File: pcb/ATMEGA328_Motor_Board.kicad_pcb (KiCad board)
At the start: 2 copper layers, 77 x 100 mm, 182 parts, among them P1 CONN_01X04, P10 CONN_01X04, P11 CONN_01X02, P12 CONN_01X03, P13 CONN_01X02, P14 USB_MINI, P15 CONN_01X02, P16 CONN_02X03, P2 CONN_01X04, P3 CONN_01X03, P4 CONN_01X03, P5 CONN_01X03, P6 CONN_01X03, P7 CONN_01X03, P8 CONN_01X03, P9 CONN_01X04, SW1 Pulsador_2p, U1 ATMEGA328, U10 VOM617A, U11 VOM617A, U12 ASSR-1218, U13 ASSR-1218, U2 PCA9685, U3 FT231X, U4 L298P, U5 L298P, U6 TSR_1, U7 LM2903, U8 LM2903, U9 VOM617A, Y1 16MHz

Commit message: finalizado conexionado de pads
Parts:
- removed the Gnd-Via at (123.2, 111.3)
- added Gnd-Via: VAL**, Vias:Gnd-Via, F.Cu at (164.8, 121.6)
- added Gnd-Via: VAL**, Vias:Gnd-Via, F.Cu at (137.4, 83.2)
- added Gnd-Via: VAL**, Vias:Gnd-Via, F.Cu at (175.9, 86.8)
- added Gnd-Via: VAL**, Vias:Gnd-Via, F.Cu at (128.4, 97.7)
- added Gnd-Via: VAL**, Vias:Gnd-Via, F.Cu at (167.9, 99.3)
- added Gnd-Via: VAL**, Vias:Gnd-Via, F.Cu at (167.9, 97.8)
- added Gnd-Via: VAL**, Vias:Gnd-Via, F.Cu at (152.7, 101.4)
- added Gnd-Via: VAL**, Vias:Gnd-Via, F.Cu at (158.1, 64.3)
- added Gnd-Via: VAL**, Vias:Gnd-Via, F.Cu at (165.6, 69.8)
- added Gnd-Via: VAL**, Vias:Gnd-Via, F.Cu at (111.3, 48.2)
- added Gnd-Via: VAL**, Vias:Gnd-Via, F.Cu at (117.1, 69.5)
- added Gnd-Via: VAL**, Vias:Gnd-Via, F.Cu at (157.6, 121.5)
- added Gnd-Via: VAL**, Vias:Gnd-Via, F.Cu at (114.8, 63.6)
- added Gnd-Via: VAL**, Vias:Gnd-Via, F.Cu at (143.9, 48.4)
- added Gnd-Via: VAL**, Vias:Gnd-Via, F.Cu at (157.0, 47.3)
- added Gnd-Via: VAL**, Vias:Gnd-Via, F.Cu at (121.7, 115.2)
- added Gnd-Via: VAL**, Vias:Gnd-Via, F.Cu at (173.9, 62.1)
- added Gnd-Via: VAL**, Vias:Gnd-Via, F.Cu at (184.0, 62.1)
- added Gnd-Via: VAL**, Vias:Gnd-Via, F.Cu at (184.0, 54.8)
- added Gnd-Via: VAL**, Vias:Gnd-Via, F.Cu at (184.0, 47.7)
- added Gnd-Via: VAL**, Vias:Gnd-Via, F.Cu at (171.6, 79.2)
- added Gnd-Via: VAL**, Vias:Gnd-Via, F.Cu at (173.6, 79.3)
- added Gnd-Via: VAL**, Vias:Gnd-Via, F.Cu at (162.7, 102.9)
- added Gnd-Via: VAL**, Vias:Gnd-Via, F.Cu at (169.7, 120.0)
- added Gnd-Via: VAL**, Vias:Gnd-Via, F.Cu at (174.0, 113.2)
- added Gnd-Via: VAL**, Vias:Gnd-Via, F.Cu at (174.1, 118.8)
- added Gnd-Via: VAL**, Vias:Gnd-Via, F.Cu at (136.4, 91.0)
- added Gnd-Via: VAL**, Vias:Gnd-Via, F.Cu at (175.6, 89.9)
- added Gnd-Via: VAL**, Vias:Gnd-Via, F.Cu at (182.2, 91.3)
- added Gnd-Via: VAL**, Vias:Gnd-Via, F.Cu at (150.0, 128.6)
- added Gnd-Via: VAL**, Vias:Gnd-Via, F.Cu at (145.8, 83.7)
- added Gnd-Via: VAL**, Vias:Gnd-Via, F.Cu at (140.9, 87.9)
- added Gnd-Via: VAL**, Vias:Gnd-Via, F.Cu at (151.1, 136.0)
- added Gnd-Via: VAL**, Vias:Gnd-Via, F.Cu at (159.7, 102.9)
- added Gnd-Via: VAL**, Vias:Gnd-Via, F.Cu at (151.1, 134.3)
- added Gnd-Via: VAL**, Vias:Gnd-Via, F.Cu at (141.8, 120.5)
- added Gnd-Via: VAL**, Vias:Gnd-Via, F.Cu at (129.2, 122.2)
- added Gnd-Via: VAL**, Vias:Gnd-Via, F.Cu at (125.0, 104.0)
- added Gnd-Via: VAL**, Vias:Gnd-Via, F.Cu at (156.2, 72.3)
- added Gnd-Via: VAL**, Vias:Gnd-Via, F.Cu at (155.4, 74.7)
- added Gnd-Via: VAL**, Vias:Gnd-Via, F.Cu at (144.1, 88.9)
- added Gnd-Via: VAL**, Vias:Gnd-Via, F.Cu at (132.1, 72.7)
- added Gnd-Via: VAL**, Vias:Gnd-Via, F.Cu at (154.2, 83.2)
- added Gnd-Via: VAL**, Vias:Gnd-Via, F.Cu at (159.1, 83.3)
- added Gnd-Via: VAL**, Vias:Gnd-Via, F.Cu at (137.0, 103.0)
- added Gnd-Via: VAL**, Vias:Gnd-Via, F.Cu at (164.4, 83.5)
- added Gnd-Via: VAL**, Vias:Gnd-Via, F.Cu at (128.3, 70.8)
- added Gnd-Via: VAL**, Vias:Gnd-Via, F.Cu at (131.3, 70.9)
- added Gnd-Via: VAL**, Vias:Gnd-Via, F.Cu at (133.0, 103.0)
- added Gnd-Via: VAL**, Vias:Gnd-Via, F.Cu at (122.3, 83.2)
- added Gnd-Via: VAL**, Vias:Gnd-Via, F.Cu at (127.3, 83.2)
- added Gnd-Via: VAL**, Vias:Gnd-Via, F.Cu at (132.3, 83.2)
- moved Gnd-Via 7.17 mm to (153.7, 105.4)
- moved R2 2.50 mm to (145.5, 71.7), turned to 90 degrees
- moved R3 2.50 mm to (148.0, 71.7), turned to 90 degrees
- moved C15 0.90 mm to (123.3, 113.6)
- moved Gnd-Via 0.76 mm to (128.4, 96.3)
- moved R23 0.45 mm to (151.4, 106.9)
- moved R15 0.13 mm to (125.1, 107.1)
- moved P5 0.07 mm to (176.8, 94.9)
- turned R4 to 90 degrees
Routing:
- net +5V: track 301.4 -> 538.4 mm, vias 4 -> 12
- net SERVO4: track 0.00 -> 75.0 mm, vias 0 -> 1
- net SERVO3: track 0.00 -> 72.7 mm, vias 0 -> 1
- net MOTOR4_EN: track 3.01 -> 75.6 mm, vias 0 -> 2
- net SERVO2: track 0.00 -> 59.1 mm, vias 0 -> 1
- net SERVO1: track 0.00 -> 58.3 mm, vias 0 -> 1
- net MOTOR3_EN: track 2.50 -> 60.0 mm, vias 0 -> 2
- net MOTOR2_EN: track 4.19 -> 50.5 mm, vias 1 -> 2
- net Motor3-: track 33.5 -> 77.9 mm, vias 0 -> 2
- net Motor4-: track 30.2 -> 70.7 mm, vias 1 -> 3
- net MOTOR3_SENSE: track 3.51 -> 43.9 mm, vias 0 -> 2
- net MOTOR4_B: track 4.63 -> 44.6 mm, vias 0 -> 2
- net /Potencia/Motor3_B_in: track 10.1 -> 47.5 mm, vias 0 -> 2
- net Motor4+: track 27.3 -> 64.1 mm, vias 0 -> 4
- net RESET: track 23.5 -> 59.8 mm
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
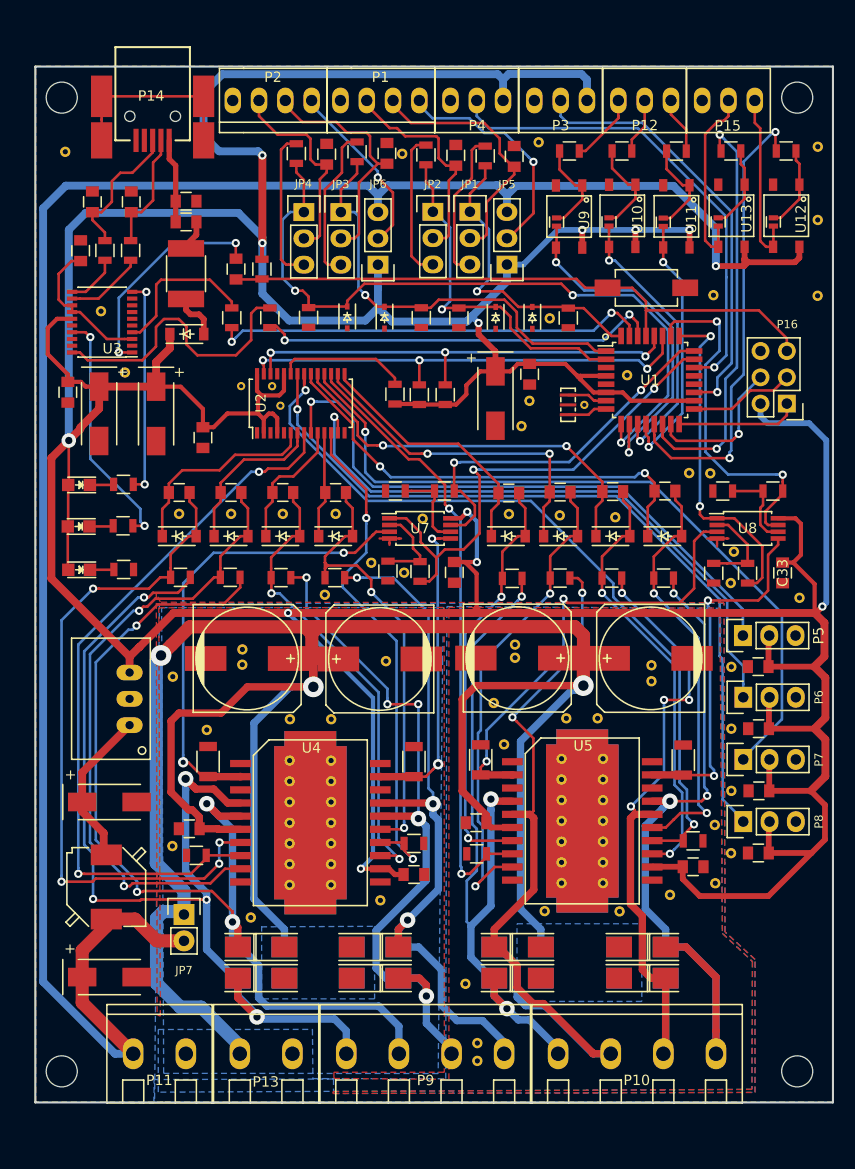
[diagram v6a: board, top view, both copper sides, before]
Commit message: añadidas referencias de componentes a las serigrafias
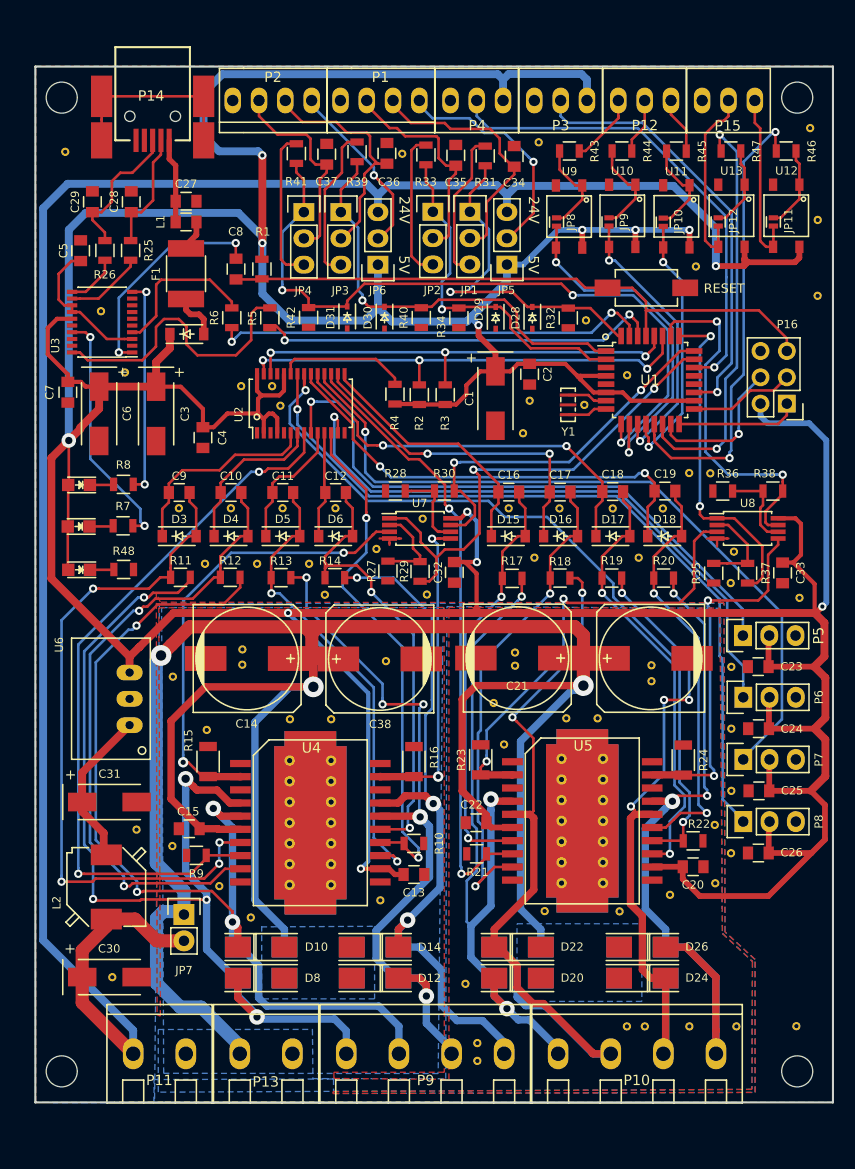
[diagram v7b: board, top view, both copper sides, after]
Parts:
- added Gnd-Via: VAL**, Vias:Gnd-Via, F.Cu at (181.9, 132.6)
- added Gnd-Via: VAL**, Vias:Gnd-Via, F.Cu at (129.9, 88.0)
- added Gnd-Via: VAL**, Vias:Gnd-Via, F.Cu at (124.8, 88.0)
- added Gnd-Via: VAL**, Vias:Gnd-Via, F.Cu at (166.7, 87.4)
- added Gnd-Via: VAL**, Vias:Gnd-Via, F.Cu at (156.6, 87.4)
- added Gnd-Via: VAL**, Vias:Gnd-Via, F.Cu at (169.0, 82.7)
- added Gnd-Via: VAL**, Vias:Gnd-Via, F.Cu at (176.1, 132.7)
- added Gnd-Via: VAL**, Vias:Gnd-Via, F.Cu at (171.6, 132.7)
- added Gnd-Via: VAL**, Vias:Gnd-Via, F.Cu at (167.3, 132.7)
- added Gnd-Via: VAL**, Vias:Gnd-Via, F.Cu at (165.6, 132.7)
- added Gnd-Via: VAL**, Vias:Gnd-Via, F.Cu at (115.9, 127.9)
- added Gnd-Via: VAL**, Vias:Gnd-Via, F.Cu at (118.2, 113.7)
- added Gnd-Via: VAL**, Vias:Gnd-Via, F.Cu at (126.2, 119.1)
- added Gnd-Via: VAL**, Vias:Gnd-Via, F.Cu at (134.9, 88.0)
- moved Gnd-Via 3.51 mm to (161.6, 64.5)
- moved Gnd-Via 3.24 mm to (172.2, 59.3)
- moved Gnd-Via 3.05 mm to (146.2, 91.0)
- moved Gnd-Via 1.95 mm to (183.2, 45.9)
- moved Gnd-Via 1.42 mm to (141.4, 86.6)
- moved Gnd-Via 0.89 mm to (164.2, 82.7)
- moved Gnd-Via 0.77 mm to (154.8, 97.8)
- moved Gnd-Via 0.77 mm to (154.8, 96.6)
- moved Gnd-Via 0.71 mm to (155.5, 75.4)
- moved Gnd-Via 0.67 mm to (159.1, 82.7)
- moved Gnd-Via 0.55 mm to (154.2, 82.7)
- moved Gnd-Via 0.54 mm to (132.3, 82.6)
- moved Gnd-Via 0.54 mm to (137.4, 82.6)
- moved Gnd-Via 0.54 mm to (122.3, 82.6)
- moved Gnd-Via 0.54 mm to (127.3, 82.6)
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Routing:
- net ENC1_A2: track 30.0 -> 34.6 mm
- net Motor1-: track 97.5 -> 95.9 mm
- net Motor2-: track 69.0 -> 70.2 mm
- net /Potencia/Motor2_B_in: track 43.2 -> 44.4 mm
- net MOTOR1_SENSE: track 45.4 -> 44.4 mm
- net +24V: track 198.4 -> 197.5 mm
- net Motor2+: track 68.7 -> 69.4 mm
- net MOTOR2_SENSE: track 30.1 -> 30.8 mm
- net ENC2_A: track 23.2 -> 22.7 mm
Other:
- board text added: "24V"
- board text added: "5V"
- board text added: "RESET"

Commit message: añadida descripcion de terminales en serigrafia
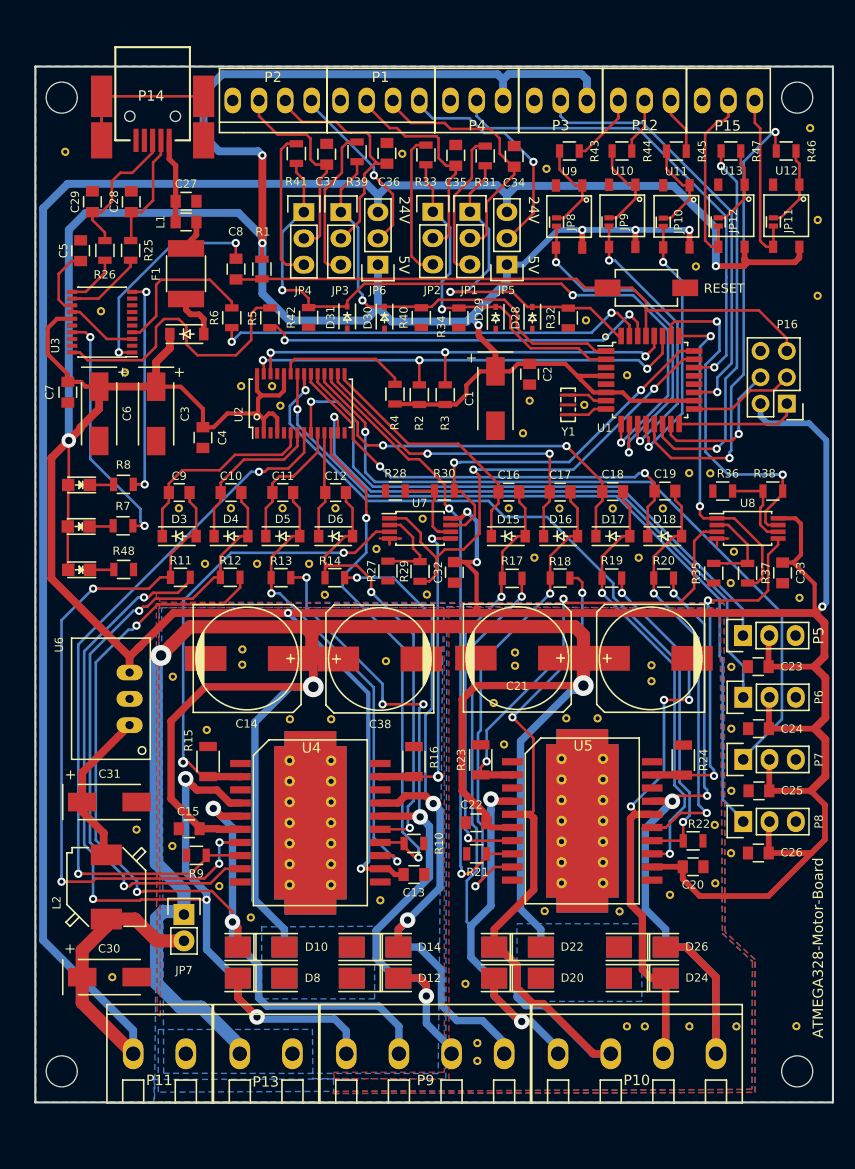
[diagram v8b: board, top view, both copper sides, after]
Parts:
- added G***: LOGO, logos:osh-logo, B.Cu at (178.8, 121.9)
- added G***: LOGO, logos:logo_HackLabAl, B.Cu at (123.3, 67.7)
- moved Gnd-Via 2.67 mm to (157.8, 49.9)
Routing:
- net uC_DO2: track 40.4 -> 37.3 mm
- net Motor1+: track 96.8 -> 99.1 mm
- net Motor3+: track 71.5 -> 73.5 mm
- net Motor2-: track 70.2 -> 71.5 mm
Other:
- board text added: "+24V"
- board text added: "A"
- board text added: "ATMEGA328-Motor-Board"
- board text added: "B"
- board text added: "CONS."
- board text added: "Cons. 1"
- board text added: "Cons. 2"
- board text added: "Ctrl. Pwr."
- board text added: "DI1"
- board text added: "DI2"
- board text added: "DI3"
- board text added: "DO1"
- board text added: "DO2"
- board text added: "Dig. In"
- board text added: "Dig. Out"
- board text added: "Encoder 1"
- board text added: "Encoder 2"
- board text added: "GND"
- board text added: "M1+"
- board text added: "M1-"
- board text added: "M2+"
- board text added: "M2-"
- board text added: "M3+"
- board text added: "M3-"
- board text added: "M4+"
- board text added: "M4-"
- board text added: "Motor 1"
- board text added: "Motor 2"
- board text added: "Motor 3"
- board text added: "Motor 4"
- board text added: "Motor Pwr."
- board text added: "PWR"
- board text added: "VCC"
